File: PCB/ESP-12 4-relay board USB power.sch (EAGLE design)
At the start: 51 parts, among them J1 OUT1, J2 OUT2, J3 IN, J4 OUT3, J5 OUT4, K1 SRD-05VDC-SL-C, K2 SRD-05VDC-SL-C, K3 SRD-05VDC-SL-C, K4 SRD-05VDC-SL-C, Q1 2N7702P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

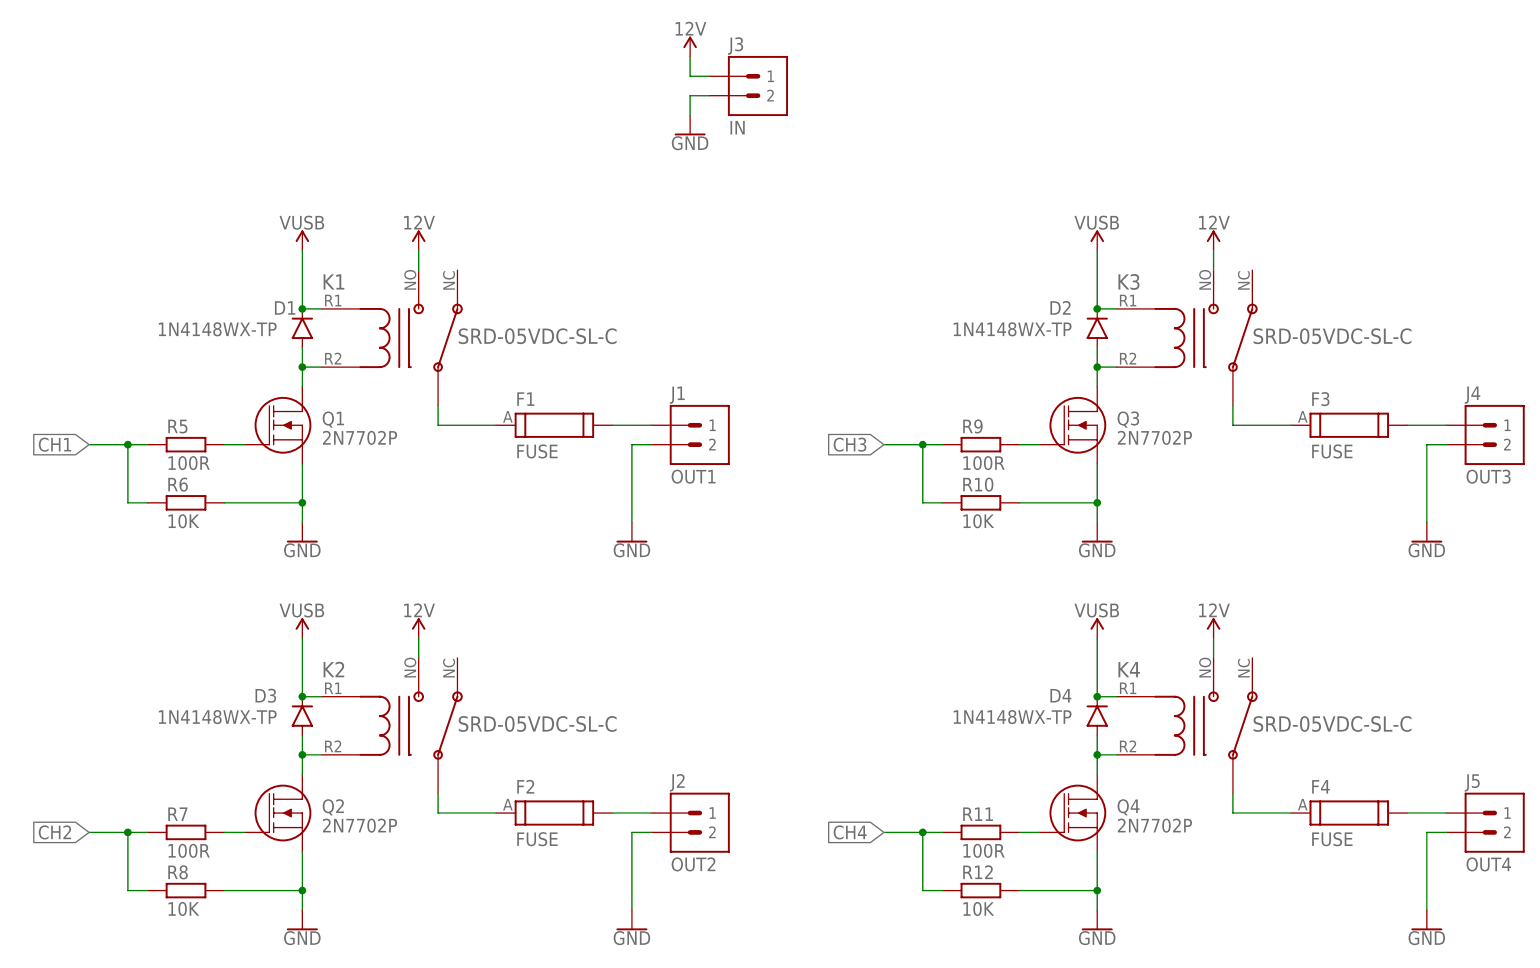
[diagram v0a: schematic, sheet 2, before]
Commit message: Switch NC and NO on relays
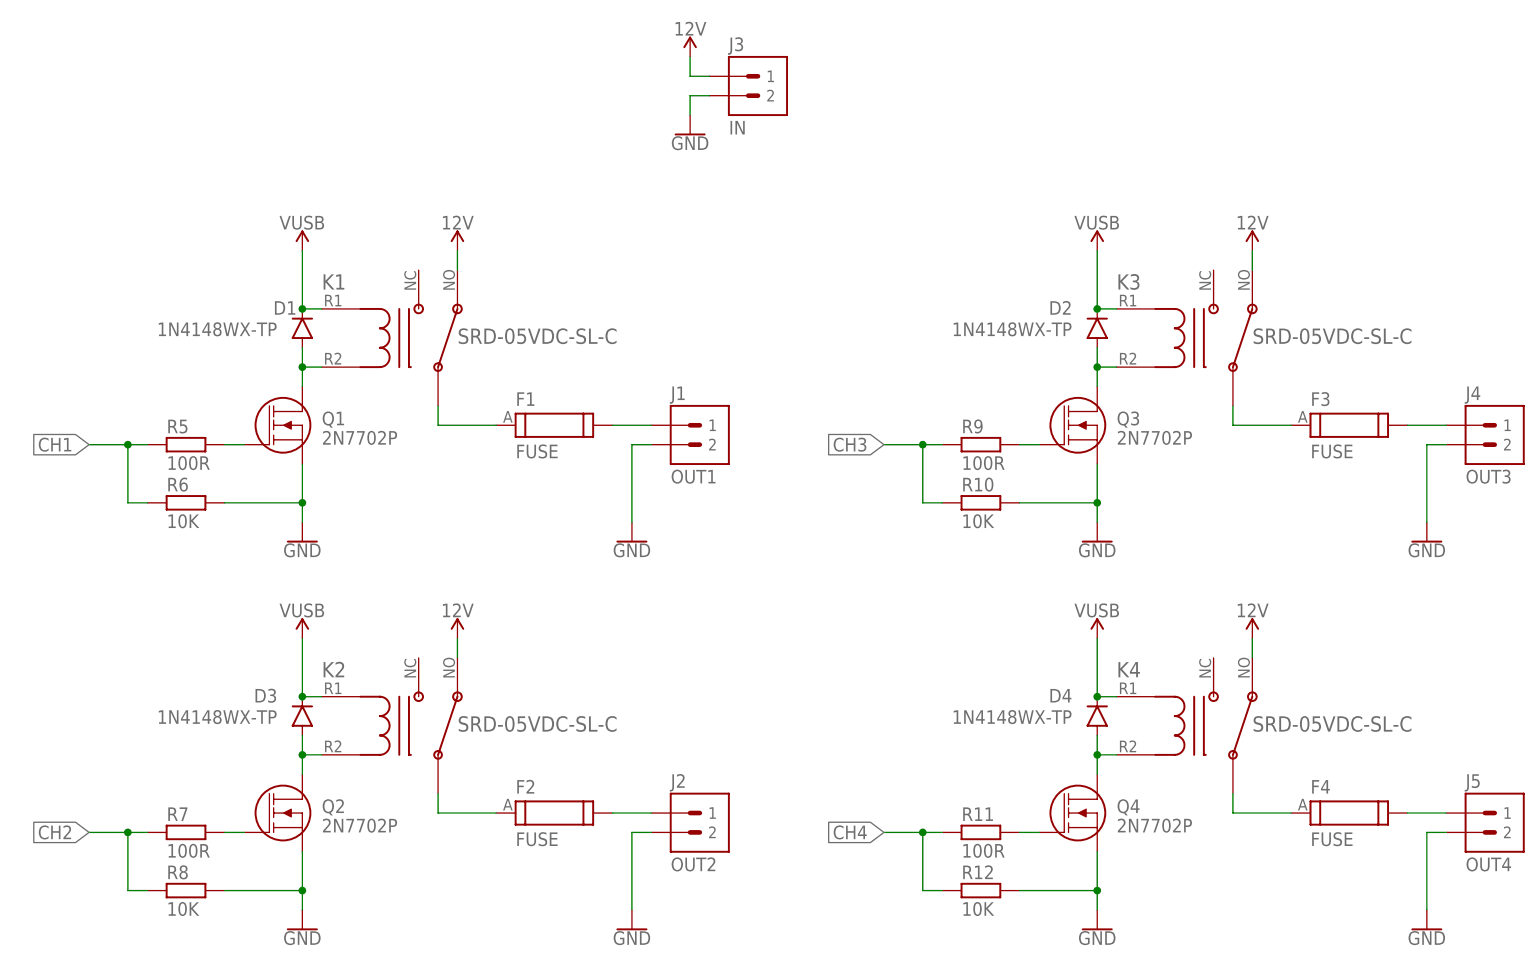
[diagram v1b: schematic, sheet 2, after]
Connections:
- net 12V: now also K1.NC, K2.NC, K3.NC, K4.NC; no longer K1.NO, K2.NO, K3.NO, K4.NO
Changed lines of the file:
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@@
 <attribute name="VALUE" x="96.52" y="99.822" size="1.778" layer="96"/>
 </instance>
-<instance part="U$3" gate="G$1" x="83.82" y="127" smashed="yes">
-<attribute name="VALUE" x="83.82" y="129.794" size="1.778" layer="96" align="bottom-center"/>
+<instance part="U$3" gate="G$1" x="88.9" y="127" smashed="yes">
+<attribute name="VALUE" x="88.9" y="129.794" size="1.778" layer="96" align="bottom-center"/>
 </instance>
 <instance part="U$4" gate="G$1" x="119.38" y="152.4" smashed="yes">
 <attribute name="VALUE" x="119.38" y="155.194" size="1.778" layer="96" align="bottom-center"/>
 </instance>
-<instance part="U$6" gate="G$1" x="187.96" y="127" smashed="yes">
-<attribute name="VALUE" x="187.96" y="129.794" size="1.778" layer="96" align="bottom-center"/>
-</instance>
-<instance part="U$7" gate="G$1" x="187.96" y="76.2" smashed="yes">
-<attribute name="VALUE" x="187.96" y="78.994" size="1.778" layer="96" align="bottom-center"/>
-</instance>
-<instance part="U$9" gate="G$1" x="83.82" y="76.2" smashed="yes">
-<attribute name="VALUE" x="83.82" y="78.994" size="1.778" layer="96" align="bottom-center"/>
+<instance part="U$6" gate="G$1" x="193.04" y="127" smashed="yes">
+<attribute name="VALUE" x="193.04" y="129.794" size="1.778" layer="96" align="bottom-center"/>
+</instance>
+<instance part="U$7" gate="G$1" x="193.04" y="76.2" smashed="yes">
+<attribute name="VALUE" x="193.04" y="78.994" size="1.778" layer="96" align="bottom-center"/>
+</instance>
+<instance part="U$9" gate="G$1" x="88.9" y="76.2" smashed="yes">
+<attribute name="VALUE" x="88.9" y="78.994" size="1.778" layer="96" align="bottom-center"/>
 </instance>
 <instance part="SUPPLY5" gate="G$1" x="68.58" y="127" smashed="yes">
@@
 <net name="12V" class="0">
 <segment>
-<pinref part="K1" gate="G$1" pin="NO"/>
-<wire x1="83.82" y1="127" x2="83.82" y2="124.46" width="0.1524" layer="91"/>
-<pinref part="U$3" gate="G$1" pin="12V"/>
-</segment>
-<segment>
 <pinref part="J3" gate="G$1" pin="1"/>
 <wire x1="119.38" y1="152.4" x2="119.38" y2="149.86" width="0.1524" layer="91"/>
@@
 </segment>
 <segment>
-<pinref part="K3" gate="G$1" pin="NO"/>
-<wire x1="187.96" y1="124.46" x2="187.96" y2="127" width="0.1524" layer="91"/>
+<pinref part="U$3" gate="G$1" pin="12V"/>
+<pinref part="K1" gate="G$1" pin="NC"/>
+<wire x1="88.9" y1="127" x2="88.9" y2="124.46" width="0.1524" layer="91"/>
+</segment>
+<segment>
+<pinref part="K3" gate="G$1" pin="NC"/>
 <pinref part="U$6" gate="G$1" pin="12V"/>
-</segment>
-<segment>
-<pinref part="K4" gate="G$1" pin="NO"/>
-<wire x1="187.96" y1="76.2" x2="187.96" y2="73.66" width="0.1524" layer="91"/>
+<wire x1="193.04" y1="124.46" x2="193.04" y2="127" width="0.1524" layer="91"/>
+</segment>
+<segment>
 <pinref part="U$7" gate="G$1" pin="12V"/>
-</segment>
-<segment>
-<pinref part="K2" gate="G$1" pin="NO"/>
-<wire x1="83.82" y1="76.2" x2="83.82" y2="73.66" width="0.1524" layer="91"/>
+<pinref part="K4" gate="G$1" pin="NC"/>
+<wire x1="193.04" y1="76.2" x2="193.04" y2="73.66" width="0.1524" layer="91"/>
+</segment>
+<segment>
 <pinref part="U$9" gate="G$1" pin="12V"/>
-</segment>
-</net>
+<pinref part="K2" gate="G$1" pin="NC"/>
+<wire x1="88.9" y1="76.2" x2="88.9" y2="73.66" width="0.1524" layer="91"/>
+</segment>
+</net>
